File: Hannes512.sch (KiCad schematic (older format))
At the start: 8 parts, among them J0 TED_SOCKET, J1 CONN_CS, J2 RAM_SELECTOR, U1 MOS_7360_TED

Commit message: Hannes256 -> Hannes512
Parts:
- J0: footprint Hannes256:DIP-48_W15.24mm_LongPads_ModSilkS -> Hannes512:DIP-48_W15.24mm_LongPads_ModSilkS
- V1: footprint Hannes256:cc_by_nc_sa -> Hannes512:cc_by_nc_sa
- V2: footprint Hannes256:logo -> Hannes512:logo
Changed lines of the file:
@@
 encoding utf-8
 Sheet 1 3
-Title "Hannes256: C16/+4 256 kB RAM Expansion"
+Title "Hannes512: C16/+4 512 kB RAM Expansion"
 Date "2023-02-27"
-Rev "3git"
+Rev "1git"
 Comp "SukkoPera"
 Comment1 "Hannes Version (Update 1 with \"TED Feature\")"
 Comment2 "Based on drawings by Solder/Synergy"
-Comment3 "Licensed under CC BY-NC-SA 4.0"
-Comment4 ""
+Comment3 "Thanks to TLC and eslapion!"
+Comment4 "Licensed under CC BY-NC-SA 4.0"
 $EndDescr
 $Sheet
@@
 F 0 "J0" H 9215 5650 50  0000 C CNN
 F 1 "TED_SOCKET" H 9215 5559 50  0000 C CNN
-F 2 "Hannes256:DIP-48_W15.24mm_LongPads_ModSilkS" H 9215 4135 50  0001 C CNN
+F 2 "Hannes512:DIP-48_W15.24mm_LongPads_ModSilkS" H 9215 4135 50  0001 C CNN
 F 3 "DOCUMENTATION" H 9215 4135 50  0001 C CNN
 	1    9215 4135
@@
 F 0 "V2" H 15618 9811 50  0000 L CNN
 F 1 "LOGO" H 15618 9720 50  0000 L CNN
-F 2 "Hannes256:logo" H 15540 9765 50  0001 C CNN
+F 2 "Hannes512:logo" H 15540 9765 50  0001 C CNN
 F 3 "" H 15540 9765 50  0001 C CNN
 	1    15540 9765
@@
 F 0 "V1" H 15618 9606 50  0000 L CNN
 F 1 "CC_LOGO" H 15618 9515 50  0000 L CNN
-F 2 "Hannes256:cc_by_nc_sa" H 15540 9560 50  0001 C CNN
+F 2 "Hannes512:cc_by_nc_sa" H 15540 9560 50  0001 C CNN
 F 3 "" H 15540 9560 50  0001 C CNN
 	1    15540 9560

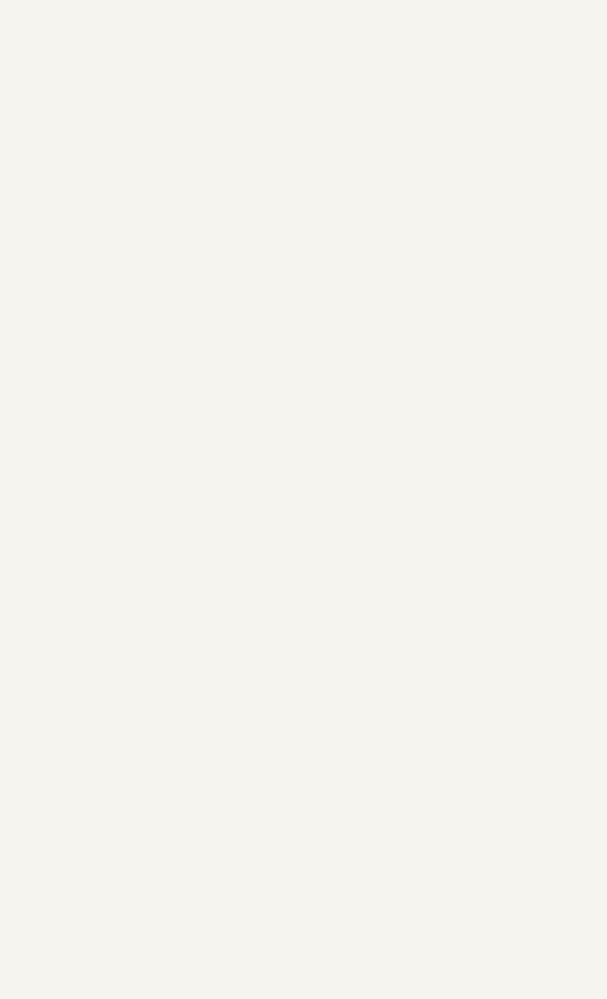
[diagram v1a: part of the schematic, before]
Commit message: Add TED Kx Protection
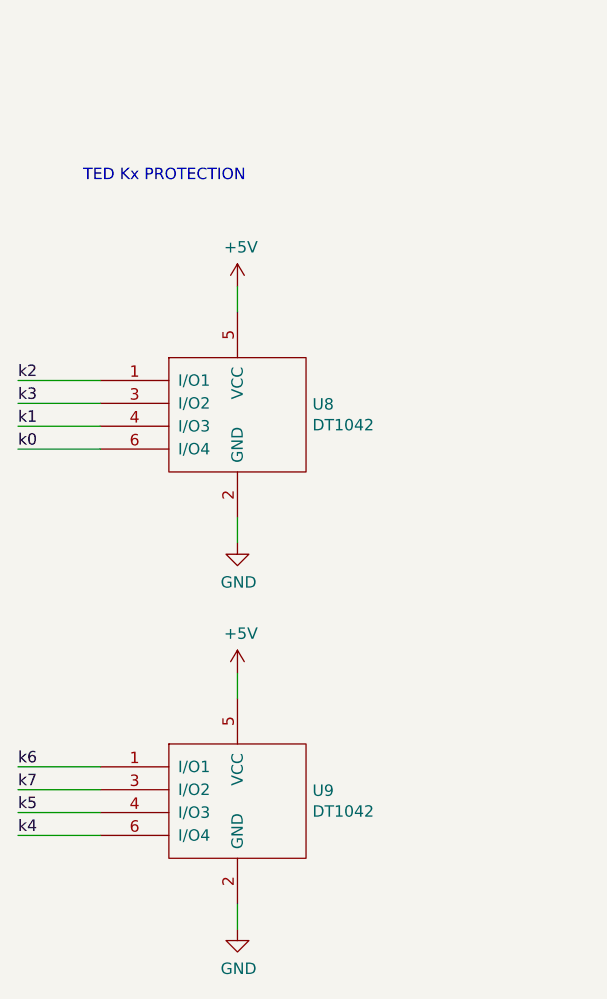
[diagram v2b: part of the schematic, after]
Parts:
- added U8, U9: DT1042, Package_SO:TSOP-6_1.65x3.05mm_P0.95mm, symbol DT1042:DT1042
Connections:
- net +5V: now also U8.5 (VCC), U9.5 (VCC)
- net GND: now also U8.2 (GND), U9.2 (GND)
- net k0: now also U8.6 (I/O4)
- net k1: now also U8.4 (I/O3)
- net k2: now also U8.1 (I/O1)
- net k3: now also U8.3 (I/O2)
- net k4: now also U9.6 (I/O4)
- net k5: now also U9.4 (I/O3)
- net k6: now also U9.1 (I/O1)
- net k7: now also U9.3 (I/O2)
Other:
- note added: "TED Kx PROTECTION"
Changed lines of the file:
@@
 	1    0    0    -1
 $EndComp
+$Comp
+L DT1042:DT1042 U8
+U 1 1 64B55A32
+P 2540 8125
+F 0 "U8" H 2868 8171 50  0000 L CNN
+F 1 "DT1042" H 2868 8080 50  0000 L CNN
+F 2 "Package_SO:TSOP-6_1.65x3.05mm_P0.95mm" H 2390 7575 50  0001 C CNN
+F 3 "" H 2390 7575 50  0001 C CNN
+	1    2540 8125
+	1    0    0    -1
+$EndComp
+Wire Wire Line
+	1940 7975 1580 7975
+Wire Wire Line
+	1940 8075 1580 8075
+Wire Wire Line
+	1940 8175 1580 8175
+Wire Wire Line
+	1940 8275 1580 8275
+Wire Wire Line
+	1940 9665 1580 9665
+Wire Wire Line
+	1940 9765 1580 9765
+Wire Wire Line
+	1940 9865 1580 9865
+Wire Wire Line
+	1940 9965 1580 9965
+Text Label 1580 8075 0    50   ~ 0
+k3
+Text Label 1580 8175 0    50   ~ 0
+k1
+Text Label 1580 8275 0    50   ~ 0
+k0
+Text Label 1580 9765 0    50   ~ 0
+k7
+$Comp
+L DT1042:DT1042 U9
+U 1 1 64B64DD4
+P 2540 9815
+F 0 "U9" H 2868 9861 50  0000 L CNN
+F 1 "DT1042" H 2868 9770 50  0000 L CNN
+F 2 "Package_SO:TSOP-6_1.65x3.05mm_P0.95mm" H 2390 9265 50  0001 C CNN
+F 3 "" H 2390 9265 50  0001 C CNN
+	1    2540 9815
+	1    0    0    -1
+$EndComp
+Wire Wire Line
+	2540 8575 2540 8685
+Wire Wire Line
+	2540 9255 2540 9365
+Wire Wire Line
+	2540 10265 2540 10375
+Wire Wire Line
+	2540 7565 2540 7675
+$Comp
+L power:+5V #PWR0101
+U 1 1 64B8CAD6
+P 2540 7565
+F 0 "#PWR0101" H 2540 7415 50  0001 C CNN
+F 1 "+5V" H 2555 7738 50  0000 C CNN
+F 2 "" H 2540 7565 50  0001 C CNN
+F 3 "" H 2540 7565 50  0001 C CNN
+	1    2540 7565
+	1    0    0    -1
+$EndComp
+$Comp
+L power:+5V #PWR0102
+U 1 1 64B8D61D
+P 2540 9255
+F 0 "#PWR0102" H 2540 9105 50  0001 C CNN
+F 1 "+5V" H 2555 9428 50  0000 C CNN
+F 2 "" H 2540 9255 50  0001 C CNN
+F 3 "" H 2540 9255 50  0001 C CNN
+	1    2540 9255
+	1    0    0    -1
+$EndComp
+$Comp
+L power:GND #PWR?
+U 1 1 64B9601A
+P 2540 8685
+AR Path="/62E48B71/64B9601A" Ref="#PWR?"  Part="1"
+AR Path="/64B9601A" Ref="#PWR0103"  Part="1"
+F 0 "#PWR0103" H 2540 8435 50  0001 C CNN
+F 1 "GND" H 2545 8512 50  0000 C CNN
+F 2 "" H 2540 8685 50  0001 C CNN
+F 3 "" H 2540 8685 50  0001 C CNN
+	1    2540 8685
+	1    0    0    -1
+$EndComp
+$Comp
+L power:GND #PWR?
+U 1 1 64B96753
+P 2540 10375
+AR Path="/62E48B71/64B96753" Ref="#PWR?"  Part="1"
+AR Path="/64B96753" Ref="#PWR0104"  Part="1"
+F 0 "#PWR0104" H 2540 10125 50  0001 C CNN
+F 1 "GND" H 2545 10202 50  0000 C CNN
+F 2 "" H 2540 10375 50  0001 C CNN
+F 3 "" H 2540 10375 50  0001 C CNN
+	1    2540 10375
+	1    0    0    -1
+$EndComp
+Text Label 1580 9665 0    50   ~ 0
+k6
+Text Label 1580 9965 0    50   ~ 0
+k4
+Text Label 1580 9865 0    50   ~ 0
+k5
+Text Label 1580 7975 0    50   ~ 0
+k2
 Wire Bus Line
 	8005 2375 8005 3085
@@
 Wire Bus Line
 	10425 2375 10425 4285
+Text Notes 1865 7110 0    50   ~ 0
+TED Kx PROTECTION
 $EndSCHEMATC

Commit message: Add part numbers
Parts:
- R1, R2: LCSC (none) -> C17414
- U8, U9: LCSC (none) -> C460064; MouserPN (none) -> 621-DT1042-04TS-7; Notes (none) -> Optional, for TED ESD protection through joystick port
- V1, V2: LCSC (none) -> -; MouserPN (none) -> -
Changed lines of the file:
@@
 F 2 "Hannes512:logo" H 15540 9765 50  0001 C CNN
 F 3 "" H 15540 9765 50  0001 C CNN
+F 4 "-" H 15540 9765 50  0001 C CNN "LCSC"
+F 5 "-" H 15540 9765 50  0001 C CNN "MouserPN"
 	1    15540 9765
 	1    0    0    -1
@@
 F 2 "Resistor_SMD:R_0805_2012Metric_Pad1.20x1.40mm_HandSolder" V 11685 3445 50  0001 C CNN
 F 3 "~" H 11755 3445 50  0001 C CNN
+F 4 "C17414" H 11755 3445 50  0001 C CNN "LCSC"
 	1    11755 3445
 	1    0    0    -1
@@
 F 2 "Resistor_SMD:R_0805_2012Metric_Pad1.20x1.40mm_HandSolder" V 11975 3445 50  0001 C CNN
 F 3 "~" H 12045 3445 50  0001 C CNN
+F 4 "C17414" H 12045 3445 50  0001 C CNN "LCSC"
 	1    12045 3445
 	1    0    0    -1
@@
 F 2 "Hannes512:cc_by_nc_sa" H 15540 9560 50  0001 C CNN
 F 3 "" H 15540 9560 50  0001 C CNN
+F 4 "-" H 15540 9560 50  0001 C CNN "LCSC"
+F 5 "-" H 15540 9560 50  0001 C CNN "MouserPN"
 	1    15540 9560
 	1    0    0    -1
@@
 F 2 "Package_SO:TSOP-6_1.65x3.05mm_P0.95mm" H 2390 7575 50  0001 C CNN
 F 3 "" H 2390 7575 50  0001 C CNN
+F 4 "C460064" H 2540 8125 50  0001 C CNN "LCSC"
+F 5 "621-DT1042-04TS-7" H 2540 8125 50  0001 C CNN "MouserPN"
+F 6 "Optional, for TED ESD protection through joystick port" H 2540 8125 50  0001 C CNN "Notes"
 	1    2540 8125
 	1    0    0    -1
@@
 F 2 "Package_SO:TSOP-6_1.65x3.05mm_P0.95mm" H 2390 9265 50  0001 C CNN
 F 3 "" H 2390 9265 50  0001 C CNN
+F 4 "C460064" H 2540 9815 50  0001 C CNN "LCSC"
+F 5 "621-DT1042-04TS-7" H 2540 9815 50  0001 C CNN "MouserPN"
+F 6 "Optional, for TED ESD protection through joystick port" H 2540 9815 50  0001 C CNN "Notes"
 	1    2540 9815
 	1    0    0    -1
@@
 Text Label 1580 7975 0    50   ~ 0
 k2
+Text Notes 1865 7110 0    50   ~ 0
+TED Kx PROTECTION
 Wire Bus Line
 	8005 2375 8005 3085
@@
 Wire Bus Line
 	10425 2375 10425 4285
-Text Notes 1865 7110 0    50   ~ 0
-TED Kx PROTECTION
 $EndSCHEMATC
